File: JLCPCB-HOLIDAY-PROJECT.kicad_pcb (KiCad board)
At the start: 2 copper layers, 44.4 x 58.9 mm, 67 parts, among them J1 USB_A_PCB, U1 CH340G, U2 STM32F030F4P6, U3 AP1117-3v3, Y1 12mhz-Crystal_GND24, Y2 12mhz-Crystal_GND24

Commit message: Added more text notes
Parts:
- moved H1 9.84 mm to (0.00, -31.5)
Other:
- board text added: "(C)2020 WingTangWong.com"
- board text added: "200 Ohm"
- board text added: "3V3"
- board text added: "AMS1117-3v3"
- board text added: "CH340G"
- board text added: "Charlieplexed"
- board text added: "GND"
- board text added: "IMU"
- board text added: "LED-R"
- board text added: "LEDS"
- board text added: "MCU"
- board text added: "QMA7981"
- board text added: "RXD"
- board text added: "STM32F030F4P6"
- board text added: "TXD"
- board text added: "USB/TTL"
- board text added: "VREG"
- board text added: "XMAS LED RING / STM32F030 / USB ORNAMENT"
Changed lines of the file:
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@@
   (general
     (thickness 1.6)
-    (drawings 8)
+    (drawings 37)
     (tracks 863)
     (zones 0)
@@
     (descr "Through hole straight pin header, 1x04, 2.54mm pitch, single row")
     (tags "Through hole pin header THT 1x04 2.54mm single row")
-    (fp_text reference SERIAL1 (at 0 2.33) (layer B.SilkS)
+    (fp_text reference SERIAL1 (at 2.61 -5.13 270) (layer B.SilkS)
       (effects (font (size 1 1) (thickness 0.15)) (justify mirror))
     )
@@
   )
   (module MountingHole:MountingHole_2.2mm_M2 (layer F.Cu)
-    (at 9.84 -31.5)
+    (at 0 -31.5)
     (descr "Mounting Hole 2.2mm, no annular, M2")
     (tags "mounting hole 2.2mm no annular m2")
@@
     )
   )
+  (gr_text "200 Ohm" (at 4.85 6.45) (layer B.SilkS)
+    (effects (font (size 1 1) (thickness 0.15)) (justify left mirror))
+  )
+  (gr_text LED-R (at 13.85 6.5) (layer B.SilkS)
+    (effects (font (size 1 1) (thickness 0.15)) (justify left mirror))
+  )
+  (gr_text AMS1117-3v3 (at 4.9 3.85) (layer B.SilkS)
+    (effects (font (size 1 1) (thickness 0.15)) (justify left mirror))
+  )
+  (gr_text VREG (at 13.75 3.8) (layer B.SilkS)
+    (effects (font (size 1 1) (thickness 0.15)) (justify left mirror))
+  )
+  (gr_text Charlieplexed (at 4.95 1.35) (layer B.SilkS)
+    (effects (font (size 1 1) (thickness 0.15)) (justify left mirror))
+  )
+  (gr_text QMA7981 (at 4.95 -1.2) (layer B.SilkS)
+    (effects (font (size 1 1) (thickness 0.15)) (justify left mirror))
+  )
+  (gr_text CH340G (at 4.95 -3.6) (layer B.SilkS)
+    (effects (font (size 1 1) (thickness 0.15)) (justify left mirror))
+  )
+  (gr_text STM32F030F4P6 (at 4.85 -6.25) (layer B.SilkS)
+    (effects (font (size 1 1) (thickness 0.15)) (justify left mirror))
+  )
+  (gr_line (start 15.24 7.62) (end -7.62 7.62) (layer B.SilkS) (width 0.12))
+  (gr_line (start 15.24 5.08) (end -7.62 5.08) (layer B.SilkS) (width 0.12))
+  (gr_line (start 15.24 2.54) (end -7.62 2.54) (layer B.SilkS) (width 0.12))
+  (gr_line (start 15.24 0) (end -7.62 0) (layer B.SilkS) (width 0.12))
+  (gr_line (start 15.24 -2.54) (end -7.62 -2.54) (layer B.SilkS) (width 0.12))
+  (gr_line (start 15.24 -5.08) (end -7.62 -5.08) (layer B.SilkS) (width 0.12))
+  (gr_line (start 5.08 -7.62) (end 5.08 10.16) (layer B.SilkS) (width 0.12))
+  (gr_line (start 15.24 -7.62) (end -7.62 -7.62) (layer B.SilkS) (width 0.12))
+  (gr_line (start 15.24 10.16) (end 15.24 -7.62) (layer B.SilkS) (width 0.12))
+  (gr_line (start -7.62 10.16) (end 15.24 10.16) (layer B.SilkS) (width 0.12))
+  (gr_line (start -7.62 -7.62) (end -7.62 10.16) (layer B.SilkS) (width 0.12))
+  (gr_text LEDS (at 13.6 1.15) (layer B.SilkS)
+    (effects (font (size 1 1) (thickness 0.15)) (justify left mirror))
+  )
+  (gr_text IMU (at 13.75 -1.3) (layer B.SilkS)
+    (effects (font (size 1 1) (thickness 0.15)) (justify left mirror))
+  )
+  (gr_text USB/TTL (at 13.9 -3.65) (layer B.SilkS)
+    (effects (font (size 1 1) (thickness 0.15)) (justify left mirror))
+  )
+  (gr_text MCU (at 14.05 -6.15) (layer B.SilkS)
+    (effects (font (size 1 1) (thickness 0.15)) (justify left mirror))
+  )
+  (gr_text GND (at -10.26 1.16) (layer B.SilkS)
+    (effects (font (size 1 1) (thickness 0.15)) (justify mirror))
+  )
+  (gr_text RXD (at -10.35 -1.4) (layer B.SilkS)
+    (effects (font (size 1 1) (thickness 0.15)) (justify mirror))
+  )
+  (gr_text TXD (at -10.58 -4.21) (layer B.SilkS)
+    (effects (font (size 1 1) (thickness 0.15)) (justify mirror))
+  )
+  (gr_text 3V3 (at -10.58 -6.89) (layer B.SilkS)
+    (effects (font (size 1 1) (thickness 0.15)) (justify mirror))
+  )
+  (gr_text "XMAS LED RING / STM32F030 / USB ORNAMENT" (at 0.59 -9.65) (layer B.SilkS)
+    (effects (font (size 1 1) (thickness 0.15)) (justify mirror))
+  )
+  (gr_text "(C)2020 WingTangWong.com" (at 1.35 13.38) (layer B.SilkS)
+    (effects (font (size 1 1) (thickness 0.15)) (justify mirror))
+  )
   (gr_circle (center 5.71 -12.29) (end 5.99 -12.29) (layer F.SilkS) (width 0.12))

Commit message: Sync
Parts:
- added 5V-IN1: Conn_01x02_Male, Connector_PinHeader_2.54mm:PinHeader_1x02_P2.54mm_Vertical, B.Cu at (8.55, -13.1)
- moved H1 3.07 mm to (1.27, -34.3)
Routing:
- net VBUS: track 62.9 -> 66.5 mm
- net Net-(D11-Pad2): track 100.4 -> 103.0 mm
- net GND: track 155.1 -> 156.6 mm
- net Net-(D1-Pad1): track 88.1 -> 89.1 mm
- net Net-(D13-Pad2): track 100.0 -> 100.6 mm
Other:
- board text added: "GITHUB"
- board text added: "WingTechCorner/XMAS-USB-ORNAMENT"
- board text removed: "AMS1117-3v3"
- board text removed: "VREG"

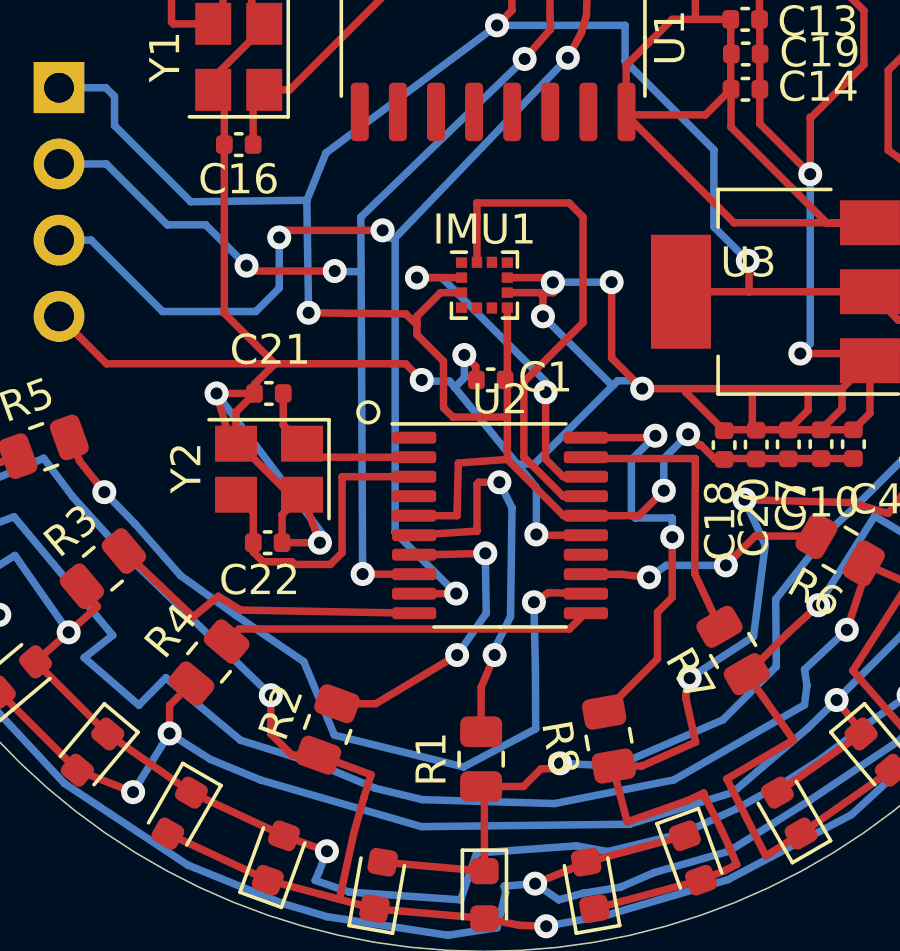
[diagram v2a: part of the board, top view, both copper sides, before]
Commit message: Updated traces to add interrupt return, address set to 0, and boot/nrst for the mcu
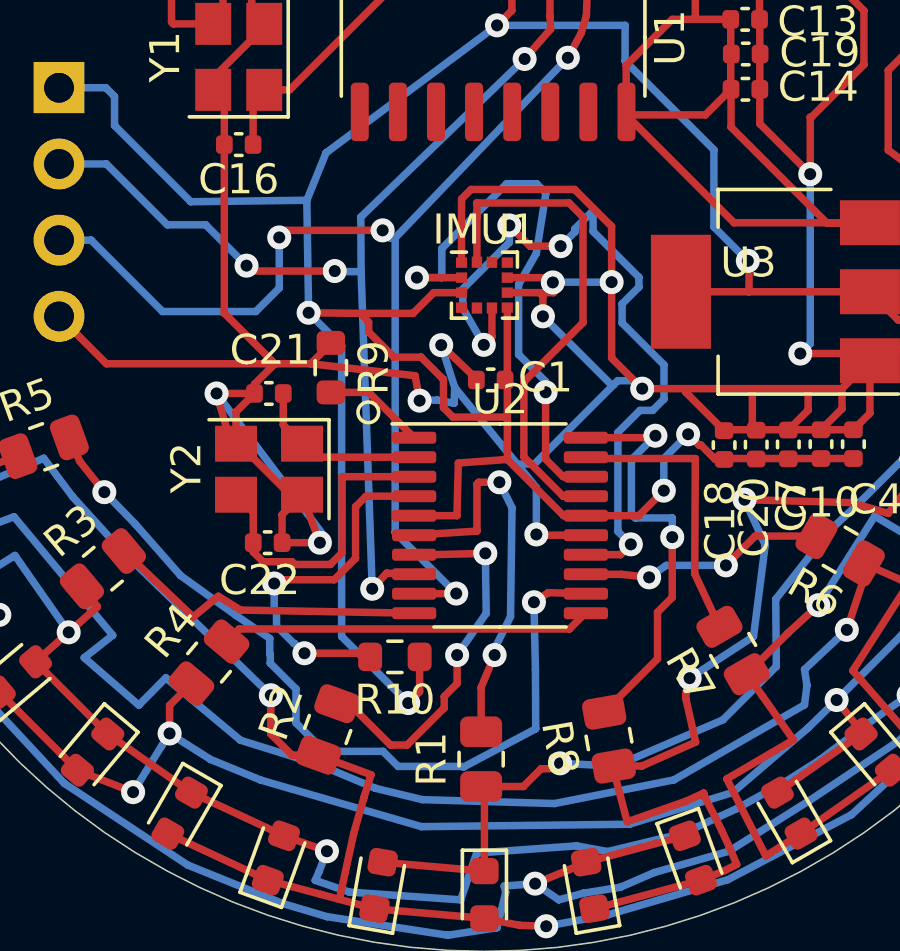
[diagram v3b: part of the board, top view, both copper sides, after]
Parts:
- added R10: 4.7KOhms-±1%-1_10W-0603, Resistor_SMD:R_0603_1608Metric, F.Cu at (-2.98, 12.4)
- added R9: 4.7KOhms-±1%-1_10W-0603, Resistor_SMD:R_0603_1608Metric, F.Cu at (-5.12, 2.75)
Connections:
- IMU1 pad 1: Net-(IMU1-Pad1) -> GND
- IMU1 pad 6: Net-(IMU1-Pad6) -> IMU-INT
- U1 pad 9: Net-(U1-Pad9) -> MCU-BOOT
- U2 pad 1: Net-(U2-Pad1) -> MCU-BOOT
- U2 pad 14: Net-(U2-Pad14) -> IMU-INT
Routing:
- net IMU-INT: track 0.00 -> 25.1 mm, vias 0 -> 4
- net 3V3: track 85.2 -> 102.5 mm, vias 5 -> 6
- net GND: track 156.6 -> 169.0 mm
- net Net-(R10-Pad2): track 0.00 -> 11.9 mm, vias 0 -> 2
- net I2C_SDA: track 11.4 -> 18.8 mm
- net MCU-BOOT: track 0.00 -> 3.40 mm
- net B: track 10.5 -> 12.7 mm
- net E: track 26.8 -> 27.7 mm
